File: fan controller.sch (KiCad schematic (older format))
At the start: 0 parts

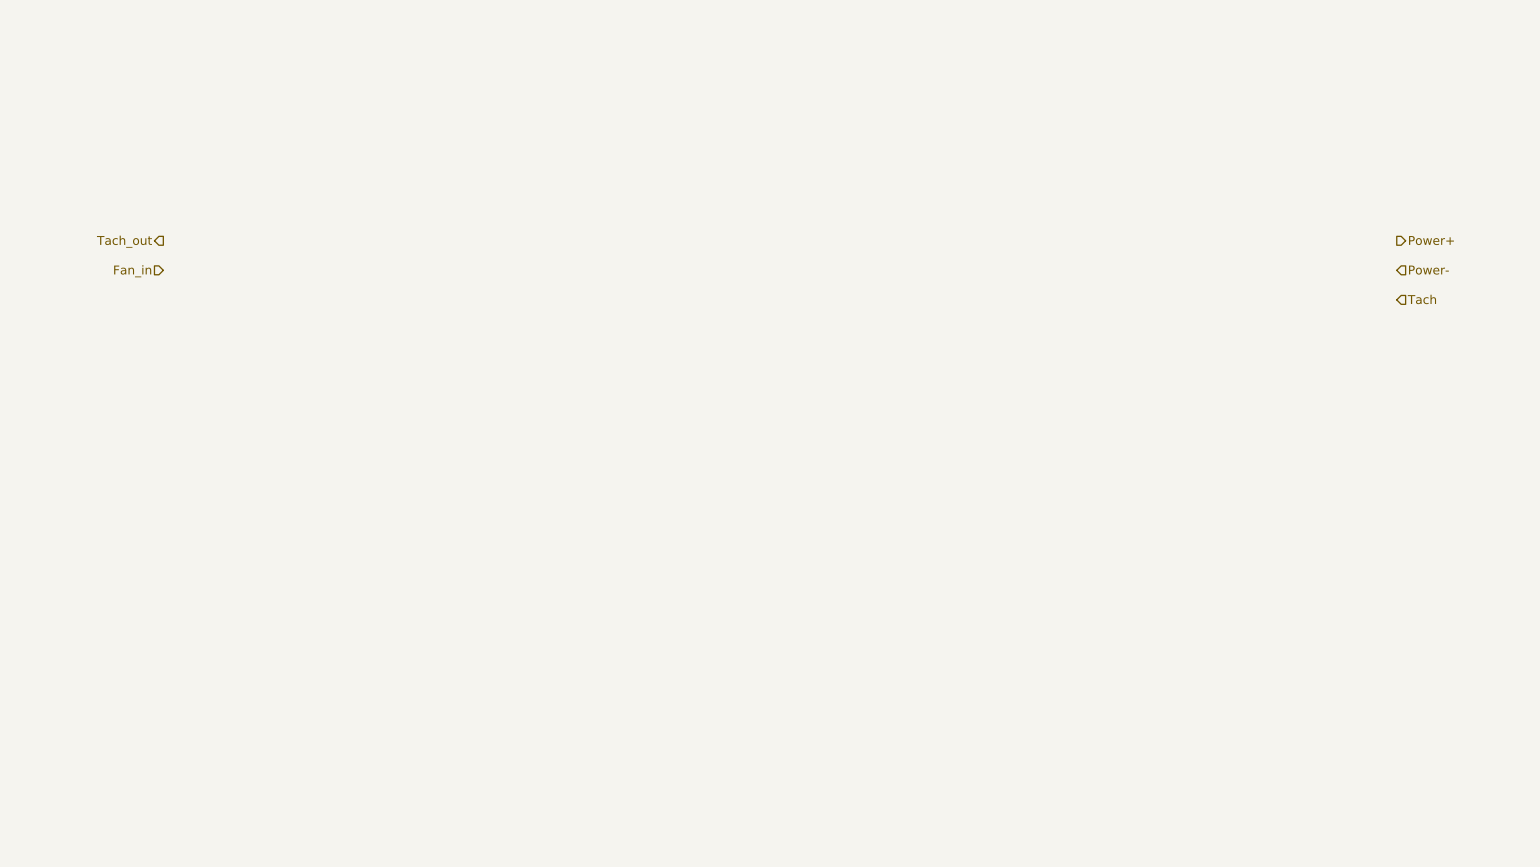
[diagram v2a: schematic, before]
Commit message: Module 3 unit 4
Understanding The Current/Fan Driver Module
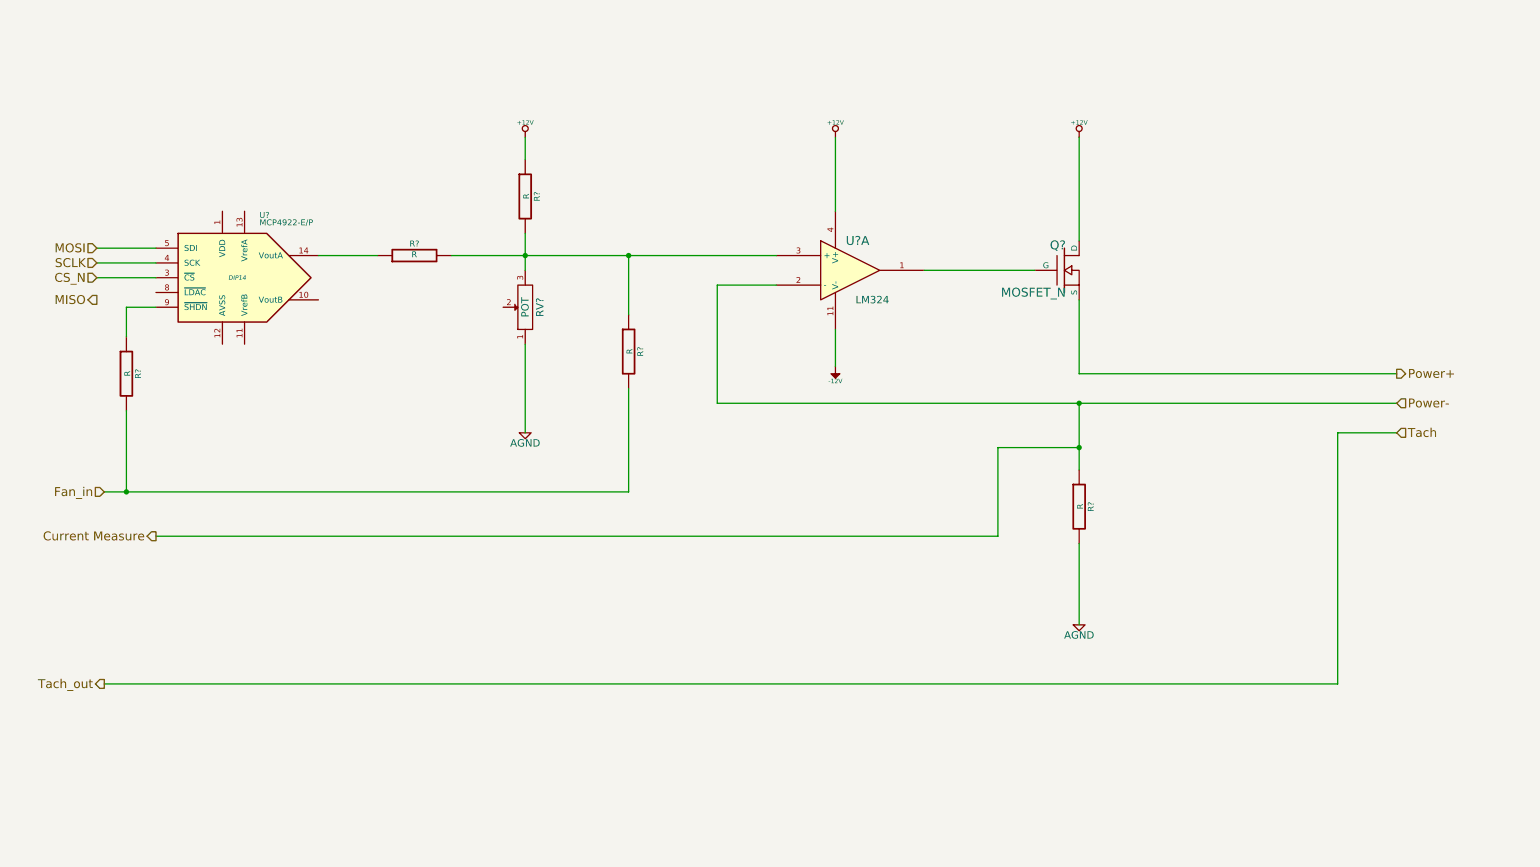
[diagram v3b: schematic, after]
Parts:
- added Q?: MOSFET_N, ~, symbol MOSFET_N
- added R? (x5): R, ~, symbol R
- added RV?: POT, ~, symbol POT
- added U?: LM324, symbol LM324
- added U?: MCP4922-E/P, DIP14, symbol MCP4922-E/P
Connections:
- net Fan_in: now also R?.2, R?.2
- net Power+: now also Q?.S
- new net: Q?.G, U?.1
- new net: R?.1, R?.2, R?.2, RV?.3, U?.3 (+)
- new net: R?.1, U?.14 (VoutA)
- new net: R?.1, U?.9 (~SHDN~)
- new net +12V: Q?.D, R?.1, U?.4 (V+)
- new net -12V: U?.11 (V-)
- new net AGND: R?.2, RV?.1
- new net CS_N: U?.3 (~CS~)
- new net Current Measure: R?.1, U?.2 (-)
- new net MOSI: U?.5 (SDI)
- new net SCLK: U?.4 (SCK)

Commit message: Module 3 Unit 9
Understanding The Arduino Module
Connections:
- net Current Measure renamed Current_Measure
- net Fan_in renamed Fan_En_N
- net Power+ renamed Fan_Out+
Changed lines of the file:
@@
 Sheet 7 9
 Title ""
-Date "15 feb 2014"
+Date "16 feb 2014"
 Rev ""
 Comp ""
@@
 $EndDescr
 Text HLabel 9800 3100 2    60   Output ~ 0
-Power+
-Text HLabel 9800 3300 2    60   Input ~ 0
-Power-
+Fan_Out+
+Text HLabel 9800 3300 2    60   Output ~ 0
+Fan_Out-
 Text HLabel 9800 3500 2    60   Input ~ 0
-Tach
+Tach_In
 Text HLabel 1050 5200 0    60   Output ~ 0
-Tach_out
+Tach_Meas
 Text HLabel 1050 3900 0    60   Input ~ 0
-Fan_in
+Fan_En_N
 $Comp
 L LM324 U?
@@
 	9400 5200 1050 5200
 Text HLabel 1400 4200 0    60   Output ~ 0
-Current Measure
+Current_Measure
 Wire Wire Line
 	7650 3600 7100 3600

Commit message: Module 3 Unit 10
Revisiting The Current/Fan Module
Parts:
- removed R? (x3): R, ~, symbol R
- removed RV?: POT, ~, symbol POT
- added D?: DIODE, ~, symbol DIODE
- added Q? (x2): MOSFET_N, ~, symbol MOSFET_N
- added TH?: THERMISTOR, ~, symbol THERMISTOR
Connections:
- net +12V: no longer Q?.D
- net AGND: now also Q?.S, Q?.S
- net Current_Measure: now also Q?.S, Q?.D
- net Fan_Out+: now also D?.2 (K), TH?.2; no longer Q?.S
- net at R?.2, U?.3 (+): now also Q?.D
- new net +12C: TH?.1
- new net FAN_MODE: Q?.G
- new net FAN_PWM: Q?.G
- new net Fan_Out-: D?.1 (A), Q?.D
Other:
- moved on the sheet: Q?, R?
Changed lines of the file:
@@
 $Descr A4 11693 8268
 encoding utf-8
-Sheet 7 9
+Sheet 6 9
 Title ""
 Date "16 feb 2014"
@@
 Comment4 ""
 $EndDescr
-Text HLabel 9800 3100 2    60   Output ~ 0
+Text HLabel 10100 1900 2    60   Output ~ 0
 Fan_Out+
-Text HLabel 9800 3300 2    60   Output ~ 0
+Text HLabel 10100 2100 2    60   Output ~ 0
 Fan_Out-
-Text HLabel 9800 3500 2    60   Input ~ 0
+Text HLabel 10100 6300 2    60   Input ~ 0
 Tach_In
-Text HLabel 1050 5200 0    60   Output ~ 0
+Text HLabel 1350 6300 0    60   Output ~ 0
 Tach_Meas
-Text HLabel 1050 3900 0    60   Input ~ 0
-Fan_En_N
+Text HLabel 1400 3900 0    60   Input ~ 0
+FAN_PWM
 $Comp
 L LM324 U?
@@
 L MOSFET_N Q?
 U 1 1 52F92320
-P 7550 2400
-F 0 "Q?" H 7560 2570 60  0000 R CNN
-F 1 "MOSFET_N" H 7560 2250 60  0000 R CNN
-F 2 "~" H 7550 2400 60  0000 C CNN
-F 3 "~" H 7550 2400 60  0000 C CNN
-	1    7550 2400
-	1    0    0    -1
-$EndComp
-$Comp
-L +12V #PWR025
-U 1 1 52F9233B
-P 7650 1500
-F 0 "#PWR025" H 7650 1450 20  0001 C CNN
-F 1 "+12V" H 7650 1600 30  0000 C CNN
-F 2 "" H 7650 1500 60  0000 C CNN
-F 3 "" H 7650 1500 60  0000 C CNN
-	1    7650 1500
-	1    0    0    -1
-$EndComp
-Wire Wire Line
-	7350 2400 6600 2400
-Wire Wire Line
-	7650 2600 7650 3100
-Wire Wire Line
-	7650 3100 9800 3100
+P 7900 2400
+F 0 "Q?" H 7910 2570 60  0000 R CNN
+F 1 "MOSFET_N" H 7910 2250 60  0000 R CNN
+F 2 "~" H 7900 2400 60  0000 C CNN
+F 3 "~" H 7900 2400 60  0000 C CNN
+	1    7900 2400
+	1    0    0    -1
+$EndComp
 $Comp
 L R R?
 U 1 1 52F92389
-P 7650 4000
-F 0 "R?" V 7730 4000 40  0000 C CNN
-F 1 "R" V 7657 4001 40  0000 C CNN
-F 2 "~" V 7580 4000 30  0000 C CNN
-F 3 "~" H 7650 4000 30  0000 C CNN
-	1    7650 4000
+P 8000 4650
+F 0 "R?" V 8080 4650 40  0000 C CNN
+F 1 "R" V 8007 4651 40  0000 C CNN
+F 2 "~" V 7930 4650 30  0000 C CNN
+F 3 "~" H 8000 4650 30  0000 C CNN
+	1    8000 4650
 	1    0    0    -1
 $EndComp
@@
 L AGND #PWR026
 U 1 1 52F923B3
-P 7650 4800
-F 0 "#PWR026" H 7650 4800 40  0001 C CNN
-F 1 "AGND" H 7650 4730 50  0000 C CNN
-F 2 "" H 7650 4800 60  0000 C CNN
-F 3 "" H 7650 4800 60  0000 C CNN
-	1    7650 4800
-	1    0    0    -1
-$EndComp
-Wire Wire Line
-	5200 3300 9800 3300
-Wire Wire Line
-	7650 3300 7650 3750
-Wire Wire Line
-	7650 4250 7650 4800
-Wire Wire Line
-	7650 1500 7650 2200
-Wire Wire Line
-	5200 3300 5200 2500
-Wire Wire Line
-	5200 2500 5600 2500
-Connection ~ 7650 3300
+P 8000 5200
+F 0 "#PWR026" H 8000 5200 40  0001 C CNN
+F 1 "AGND" H 8000 5130 50  0000 C CNN
+F 2 "" H 8000 5200 60  0000 C CNN
+F 3 "" H 8000 5200 60  0000 C CNN
+	1    8000 5200
+	1    0    0    -1
+$EndComp
 $Comp
 L +12V #PWR027
@@
 Wire Wire Line
 	6000 2800 6000 3050
-$Comp
-L R R?
-U 1 1 52F9247C
-P 3900 1900
-F 0 "R?" V 3980 1900 40  0000 C CNN
-F 1 "R" V 3907 1901 40  0000 C CNN
-F 2 "~" V 3830 1900 30  0000 C CNN
-F 3 "~" H 3900 1900 30  0000 C CNN
-	1    3900 1900
-	1    0    0    -1
-$EndComp
-$Comp
-L +12V #PWR029
-U 1 1 52F924A2
-P 3900 1500
-F 0 "#PWR029" H 3900 1450 20  0001 C CNN
-F 1 "+12V" H 3900 1600 30  0000 C CNN
-F 2 "" H 3900 1500 60  0000 C CNN
-F 3 "" H 3900 1500 60  0000 C CNN
-	1    3900 1500
-	1    0    0    -1
-$EndComp
-$Comp
-L POT RV?
-U 1 1 52F924BF
-P 3900 2650
-F 0 "RV?" H 3900 2550 50  0000 C CNN
-F 1 "POT" H 3900 2650 50  0000 C CNN
-F 2 "~" H 3900 2650 60  0000 C CNN
-F 3 "~" H 3900 2650 60  0000 C CNN
-	1    3900 2650
-	0    -1   -1   0
-$EndComp
-Wire Wire Line
-	3900 1650 3900 1500
 Wire Wire Line
 	3400 2300 5600 2300
-Wire Wire Line
-	3900 2150 3900 2400
-Connection ~ 3900 2300
 $Comp
 L AGND #PWR030
 U 1 1 52F924FA
-P 3900 3500
-F 0 "#PWR030" H 3900 3500 40  0001 C CNN
-F 1 "AGND" H 3900 3430 50  0000 C CNN
-F 2 "" H 3900 3500 60  0000 C CNN
-F 3 "" H 3900 3500 60  0000 C CNN
-	1    3900 3500
-	1    0    0    -1
-$EndComp
-Wire Wire Line
-	3900 3500 3900 2900
+P 4600 3500
+F 0 "#PWR030" H 4600 3500 40  0001 C CNN
+F 1 "AGND" H 4600 3430 50  0000 C CNN
+F 2 "" H 4600 3500 60  0000 C CNN
+F 3 "" H 4600 3500 60  0000 C CNN
+	1    4600 3500
+	1    0    0    -1
+$EndComp
 $Comp
 L MCP4922-E/P U?
@@
 	1    0    0    -1
 $EndComp
-Wire Wire Line
-	9800 3500 9400 3500
-Wire Wire Line
-	9400 3500 9400 5200
-Wire Wire Line
-	9400 5200 1050 5200
 Text HLabel 1400 4200 0    60   Output ~ 0
 Current_Measure
-Wire Wire Line
-	7650 3600 7100 3600
-Wire Wire Line
-	7100 3600 7100 4200
-Wire Wire Line
-	7100 4200 1400 4200
-Connection ~ 7650 3600
-$Comp
-L R R?
-U 1 1 52F92650
-P 4600 2950
-F 0 "R?" V 4680 2950 40  0000 C CNN
-F 1 "R" V 4607 2951 40  0000 C CNN
-F 2 "~" V 4530 2950 30  0000 C CNN
-F 3 "~" H 4600 2950 30  0000 C CNN
-	1    4600 2950
-	1    0    0    -1
-$EndComp
-Wire Wire Line
-	1050 3900 4600 3900
-Wire Wire Line
-	4600 3900 4600 3200
-Wire Wire Line
-	4600 2700 4600 2300
-Connection ~ 4600 2300
 $Comp
 L R R?
@@
 	1400 2450 1000 2450
 $Comp
-L R R?
-U 1 1 52F927E7
-P 1200 3100
-F 0 "R?" V 1280 3100 40  0000 C CNN
-F 1 "R" V 1207 3101 40  0000 C CNN
-F 2 "~" V 1130 3100 30  0000 C CNN
-F 3 "~" H 1200 3100 30  0000 C CNN
-	1    1200 3100
-	1    0    0    -1
-$EndComp
-Wire Wire Line
-	1400 2650 1200 2650
-Wire Wire Line
-	1200 2650 1200 2850
-Wire Wire Line
-	1200 3350 1200 3900
-Connection ~ 1200 3900
+L THERMISTOR TH?
+U 1 1 5300E1A7
+P 8000 1150
+F 0 "TH?" V 8100 1200 50  0000 C CNN
+F 1 "THERMISTOR" V 7900 1150 50  0000 C CNN
+F 2 "~" H 8000 1150 60  0000 C CNN
+F 3 "~" H 8000 1150 60  0000 C CNN
+	1    8000 1150
+	1    0    0    -1
+$EndComp
+$Comp
+L MOSFET_N Q?
+U 1 1 5300E1C8
+P 7300 4600
+F 0 "Q?" H 7310 4770 60  0000 R CNN
+F 1 "MOSFET_N" H 7310 4450 60  0000 R CNN
+F 2 "~" H 7300 4600 60  0000 C CNN
+F 3 "~" H 7300 4600 60  0000 C CNN
+	1    7300 4600
+	1    0    0    -1
+$EndComp
+Wire Wire Line
+	6600 2400 7700 2400
+Wire Wire Line
+	7400 2100 10100 2100
+Wire Wire Line
+	8000 2100 8000 2200
+$Comp
+L DIODE D?
+U 1 1 5300E25A
+P 7400 1800
+F 0 "D?" H 7400 1900 40  0000 C CNN
+F 1 "DIODE" H 7400 1700 40  0000 C CNN
+F 2 "~" H 7400 1800 60  0000 C CNN
+F 3 "~" H 7400 1800 60  0000 C CNN
+	1    7400 1800
+	0    -1   -1   0
+$EndComp
+Wire Wire Line
+	8000 800  8000 900
+Wire Wire Line
+	8000 1400 8000 1900
+Wire Wire Line
+	8000 1900 10100 1900
+Wire Wire Line
+	7400 2100 7400 2000
+Connection ~ 8000 2100
+Wire Wire Line
+	7400 1600 7400 1500
+Wire Wire Line
+	7400 1500 8000 1500
+Connection ~ 8000 1500
+Wire Wire Line
+	5600 2500 5400 2500
+Wire Wire Line
+	5400 2500 5400 3400
+Wire Wire Line
+	5400 3400 8000 3400
+Connection ~ 8000 3400
+Wire Wire Line
+	8000 5200 8000 4900
+Wire Wire Line
+	8000 2600 8000 4400
+Wire Wire Line
+	1400 4200 8000 4200
+Connection ~ 8000 4200
+Wire Wire Line
+	7400 4400 7400 4300
+Wire Wire Line
+	7400 4300 8000 4300
+Connection ~ 8000 4300
+Wire Wire Line
+	8000 5000 7400 5000
+Wire Wire Line
+	7400 5000 7400 4800
+Connection ~ 8000 5000
+$Comp
+L MOSFET_N Q?
+U 1 1 5300E4FC
+P 4500 2700
+F 0 "Q?" H 4510 2870 60  0000 R CNN
+F 1 "MOSFET_N" H 4510 2550 60  0000 R CNN
+F 2 "~" H 4500 2700 60  0000 C CNN
+F 3 "~" H 4500 2700 60  0000 C CNN
+	1    4500 2700
+	1    0    0    -1
+$EndComp
+Wire Wire Line
+	4600 2500 4600 2300
+Connection ~ 4600 2300
+Wire Wire Line
+	4600 3500 4600 2900
+Wire Wire Line
+	3100 3900 3100 2700
+Wire Wire Line
+	3100 2700 4300 2700
+Wire Wire Line
+	1400 3900 3100 3900
+Wire Wire Line
+	1350 6300 10100 6300
+Text HLabel 1400 4600 0    60   Input ~ 0
+FAN_MODE
+Wire Wire Line
+	1400 4600 7100 4600
+$Comp
+L +12C #PWR?
+U 1 1 5300F045
+P 8000 800
+F 0 "#PWR?" H 8000 770 30  0001 C CNN
+F 1 "+12C" H 8000 910 40  0000 C CNN
+F 2 "" H 8000 800 60  0000 C CNN
+F 3 "" H 8000 800 60  0000 C CNN
+	1    8000 800
+	1    0    0    -1
+$EndComp
 $EndSCHEMATC
